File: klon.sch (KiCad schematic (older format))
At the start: 71 parts, among them SW1 SW_DPDT_x2, U1 TL072, U2 LTC1044, U3 TL072

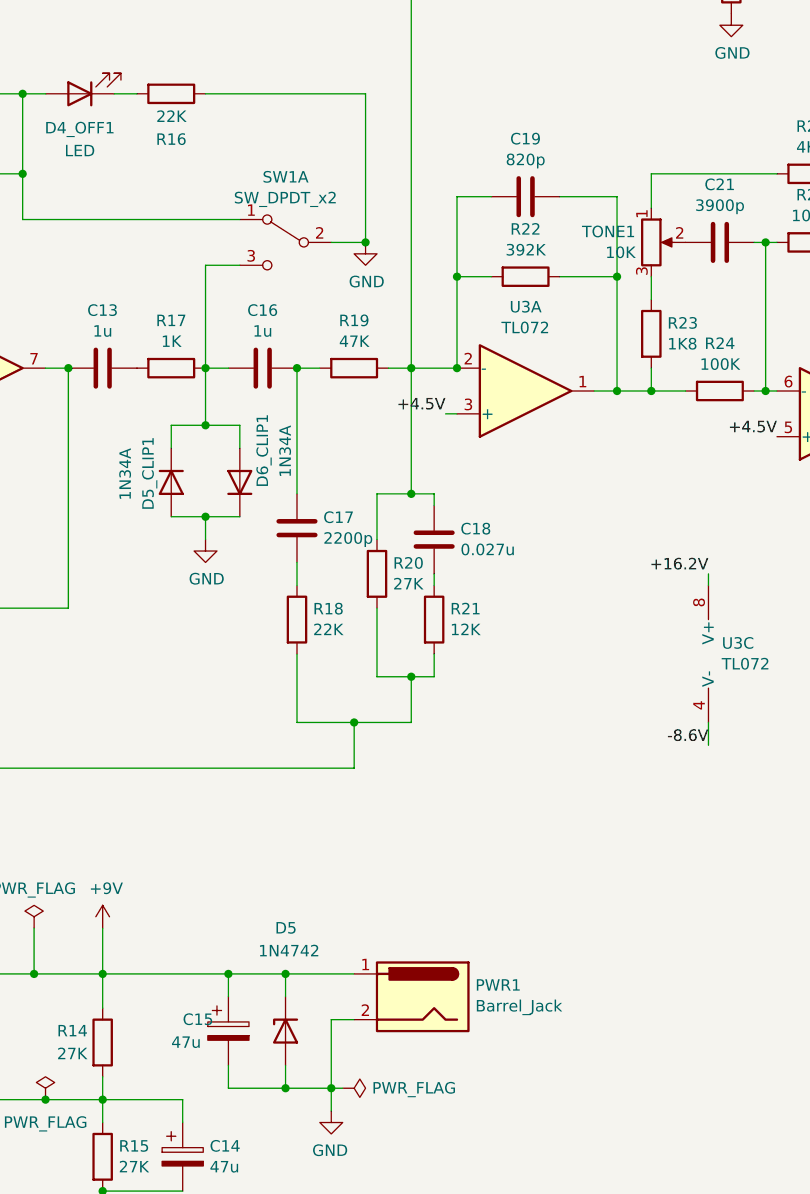
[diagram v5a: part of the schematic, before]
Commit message: fix power polarity, new PCB layout
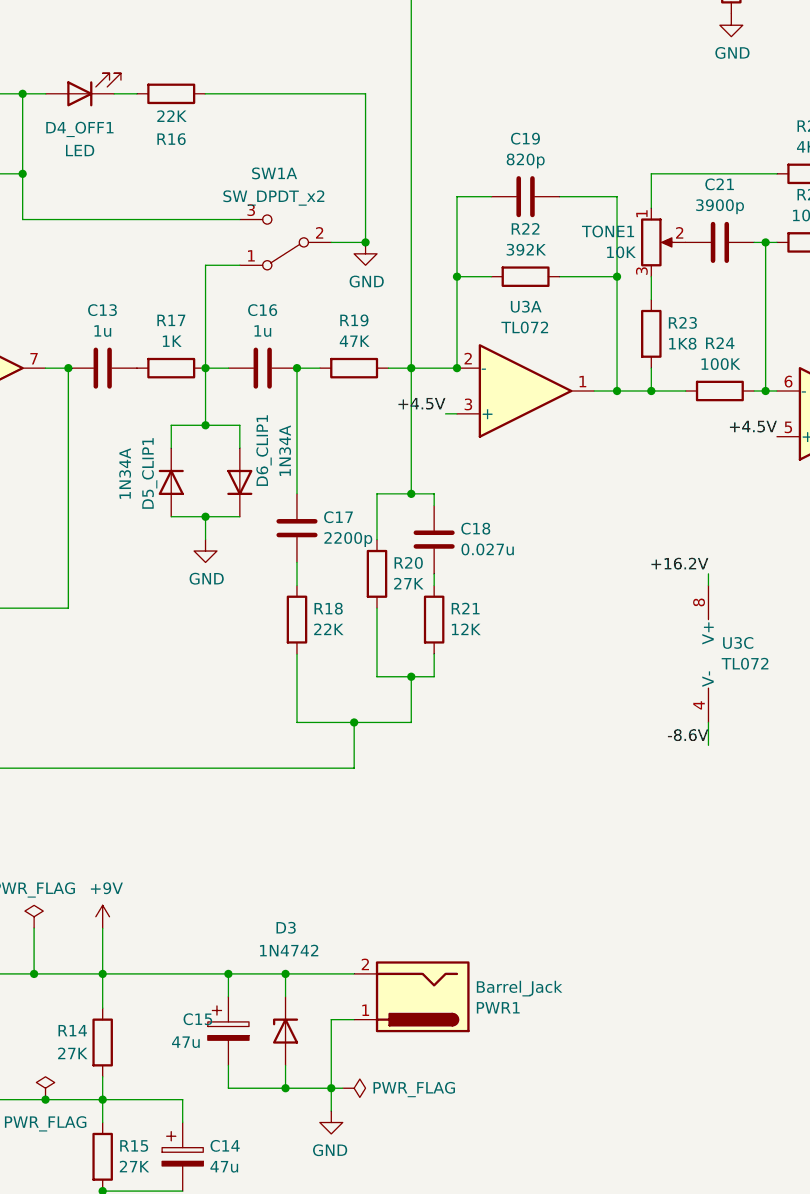
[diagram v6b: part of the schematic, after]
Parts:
- C8: footprint Capacitor_THT:C_Rect_L7.0mm_W3.5mm_P5.00mm -> Capacitor_THT:C_Rect_L7.0mm_W2.0mm_P5.00mm
- D3: renamed from D5; footprint Diode_THT:D_DO-34_SOD68_P7.62mm_Horizontal -> Diode_THT:D_DO-34_SOD68_P10.16mm_Horizontal
- GAIN_1: footprint Potentiometer_THT:Potentiometer_Alpha_RD902F-40-00D_Dual_Vertical_CircularHoles -> Connector_PinHeader_2.54mm:PinHeader_2x03_P2.54mm_Vertical
- SW1: footprint Connector_PinHeader_1.27mm:PinHeader_2x03_P1.27mm_Vertical -> Connector_PinHeader_2.54mm:PinHeader_2x03_P2.54mm_Vertical
- TONE1, VOL1: footprint Potentiometer_THT:Potentiometer_Alpha_RD901F-40-00D_Single_Vertical_CircularHoles -> Connector_PinHeader_2.54mm:PinHeader_1x03_P2.54mm_Vertical
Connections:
- net +9V: now also PWR1.2; no longer PWR1.1
- net GND: now also PWR1.1; no longer PWR1.2
- net at C16.2, D5_CLIP1.1 (K), D6_CLIP1.2 (A)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: now also SW1.1 (A); no longer SW1.3 (C)
- net at D4_OFF1.2 (A), R12.2, R13.1: now also SW1.3 (C); no longer SW1.1 (A)
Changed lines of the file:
@@
 F 0 "C8" V 2898 2950 50  0000 C CNN
 F 1 "0.068u" V 2989 2950 50  0000 C CNN
-F 2 "Capacitor_THT:C_Rect_L7.0mm_W3.5mm_P5.00mm" H 3188 2800 50  0001 C CNN
+F 2 "Capacitor_THT:C_Rect_L7.0mm_W2.0mm_P5.00mm" H 3188 2800 50  0001 C CNN
 F 3 "~" H 3150 2950 50  0001 C CNN
 	1    3150 2950
@@
 F 0 "GAIN_1" H 3281 4846 50  0000 R CNN
 F 1 "100K" H 3281 4755 50  0000 R CNN
-F 2 "Potentiometer_THT:Potentiometer_Alpha_RD902F-40-00D_Dual_Vertical_CircularHoles" H 3350 4800 50  0001 C CNN
+F 2 "Connector_PinHeader_2.54mm:PinHeader_2x03_P2.54mm_Vertical" H 3350 4800 50  0001 C CNN
 F 3 "~" H 3350 4800 50  0001 C CNN
 	1    3350 4800
@@
 $EndComp
 $Comp
-L power:GND #PWR07
+L power:GND #PWR06
 U 1 1 60CF8CE7
 P 3250 1750
-F 0 "#PWR07" H 3250 1500 50  0001 C CNN
+F 0 "#PWR06" H 3250 1500 50  0001 C CNN
 F 1 "GND" H 3255 1577 50  0000 C CNN
 F 2 "" H 3250 1750 50  0001 C CNN
@@
 F 0 "TONE1" H 7631 2546 50  0000 R CNN
 F 1 "10K" H 7631 2455 50  0000 R CNN
-F 2 "Potentiometer_THT:Potentiometer_Alpha_RD901F-40-00D_Single_Vertical_CircularHoles" H 7700 2500 50  0001 C CNN
+F 2 "Connector_PinHeader_2.54mm:PinHeader_1x03_P2.54mm_Vertical" H 7700 2500 50  0001 C CNN
 F 3 "~" H 7700 2500 50  0001 C CNN
 	1    7700 2500
@@
 F 0 "VOL1" H 9431 3546 50  0000 R CNN
 F 1 "10K" H 9431 3455 50  0000 R CNN
-F 2 "Potentiometer_THT:Potentiometer_Alpha_RD901F-40-00D_Single_Vertical_CircularHoles" H 9500 3500 50  0001 C CNN
+F 2 "Connector_PinHeader_2.54mm:PinHeader_1x03_P2.54mm_Vertical" H 9500 3500 50  0001 C CNN
 F 3 "~" H 9500 3500 50  0001 C CNN
 	1    9500 3500
@@
 $EndComp
 $Comp
-L power:GND #PWR016
+L power:GND #PWR015
 U 1 1 60DC01EF
 P 9500 3750
-F 0 "#PWR016" H 9500 3500 50  0001 C CNN
+F 0 "#PWR015" H 9500 3500 50  0001 C CNN
 F 1 "GND" H 9505 3577 50  0000 C CNN
 F 2 "" H 9500 3750 50  0001 C CNN
@@
 Connection ~ 8050 1100
 $Comp
-L power:GND #PWR015
+L power:GND #PWR014
 U 1 1 60E2597F
 P 8050 1500
-F 0 "#PWR015" H 8050 1250 50  0001 C CNN
+F 0 "#PWR014" H 8050 1250 50  0001 C CNN
 F 1 "GND" H 8055 1327 50  0000 C CNN
 F 2 "" H 8050 1500 50  0001 C CNN
@@
 $EndComp
 $Comp
-L power:GND #PWR017
+L power:GND #PWR016
 U 1 1 60E40ABE
 P 10500 4000
-F 0 "#PWR017" H 10500 3750 50  0001 C CNN
+F 0 "#PWR016" H 10500 3750 50  0001 C CNN
 F 1 "GND" H 10505 3827 50  0000 C CNN
 F 2 "" H 10500 4000 50  0001 C CNN
@@
 	5600 3700 5750 3700
 $Comp
-L power:GND #PWR012
+L power:GND #PWR011
 U 1 1 60CDC483
 P 5750 3800
-F 0 "#PWR012" H 5750 3550 50  0001 C CNN
+F 0 "#PWR011" H 5750 3550 50  0001 C CNN
 F 1 "GND" H 5755 3627 50  0000 C CNN
 F 2 "" H 5750 3800 50  0001 C CNN
@@
 	10300 3400 10500 3400
 $Comp
-L power:GND #PWR013
+L power:GND #PWR012
 U 1 1 6116E861
 P 6300 6300
-F 0 "#PWR013" H 6300 6050 50  0001 C CNN
+F 0 "#PWR012" H 6300 6050 50  0001 C CNN
 F 1 "GND" H 6305 6127 50  0000 C CNN
 F 2 "" H 6300 6300 50  0001 C CNN
@@
 $EndComp
 $Comp
-L Device:D_Zener D5
+L Device:D_Zener D3
 U 1 1 6117C2F3
 P 6100 5950
-F 0 "D5" V 5650 5900 50  0000 L CNN
+F 0 "D3" V 5650 5900 50  0000 L CNN
 F 1 "1N4742" V 5750 5800 50  0000 L CNN
-F 2 "Diode_THT:D_DO-34_SOD68_P7.62mm_Horizontal" H 6100 5950 50  0001 C CNN
+F 2 "Diode_THT:D_DO-34_SOD68_P10.16mm_Horizontal" H 6100 5950 50  0001 C CNN
 F 3 "~" H 6100 5950 50  0001 C CNN
 	1    6100 5950
@@
 $EndComp
 $Comp
-L power:GND #PWR05
+L power:GND #PWR04
 U 1 1 612C633A
 P 1850 7050
-F 0 "#PWR05" H 1850 6800 50  0001 C CNN
+F 0 "#PWR04" H 1850 6800 50  0001 C CNN
 F 1 "GND" H 1855 6877 50  0000 C CNN
 F 2 "" H 1850 7050 50  0001 C CNN
@@
 	4450 6750 3150 6750
 $Comp
-L power:GND #PWR06
+L power:GND #PWR05
 U 1 1 6132C604
 P 2200 6100
-F 0 "#PWR06" H 2200 5850 50  0001 C CNN
+F 0 "#PWR05" H 2200 5850 50  0001 C CNN
 F 1 "GND" H 2205 5927 50  0000 C CNN
 F 2 "" H 2200 6100 50  0001 C CNN
@@
 $EndComp
 $Comp
-L power:GND #PWR011
+L power:GND #PWR010
 U 1 1 6139B14F
 P 5300 6750
-F 0 "#PWR011" H 5300 6500 50  0001 C CNN
+F 0 "#PWR010" H 5300 6500 50  0001 C CNN
 F 1 "GND" H 5305 6577 50  0000 C CNN
 F 2 "" H 5300 6750 50  0001 C CNN
@@
 +4.5V
 $Comp
-L power:+9V #PWR010
+L power:+9V #PWR09
 U 1 1 614332A8
 P 5300 5500
-F 0 "#PWR010" H 5300 5350 50  0001 C CNN
+F 0 "#PWR09" H 5300 5350 50  0001 C CNN
 F 1 "+9V" H 5315 5673 50  0000 C CNN
 F 2 "" H 5300 5500 50  0001 C CNN
@@
 	4450 5700 4450 6750
 $Comp
-L power:GND #PWR08
+L power:GND #PWR07
 U 1 1 6154C007
 P 3850 6400
-F 0 "#PWR08" H 3850 6150 50  0001 C CNN
+F 0 "#PWR07" H 3850 6150 50  0001 C CNN
 F 1 "GND" H 3855 6227 50  0000 C CNN
 F 2 "" H 3850 6400 50  0001 C CNN
@@
 F 0 "SW1" H 10000 3075 50  0000 C CNN
 F 1 "SW_DPDT_x2" H 10000 3166 50  0000 C CNN
-F 2 "Connector_PinHeader_1.27mm:PinHeader_2x03_P1.27mm_Vertical" H 10000 3400 50  0001 C CNN
+F 2 "Connector_PinHeader_2.54mm:PinHeader_2x03_P2.54mm_Vertical" H 10000 3400 50  0001 C CNN
 F 3 "~" H 10000 3400 50  0001 C CNN
 	2    10000 3400
@@
 U 1 1 6160C4D4
 P 6100 2500
-F 0 "SW1" H 6100 2785 50  0000 C CNN
-F 1 "SW_DPDT_x2" H 6100 2694 50  0000 C CNN
-F 2 "Connector_PinHeader_1.27mm:PinHeader_2x03_P1.27mm_Vertical" H 6100 2500 50  0001 C CNN
+F 0 "SW1" H 6150 2200 50  0000 C CNN
+F 1 "SW_DPDT_x2" H 6150 2300 50  0000 C CNN
+F 2 "Connector_PinHeader_2.54mm:PinHeader_2x03_P2.54mm_Vertical" H 6100 2500 50  0001 C CNN
 F 3 "~" H 6100 2500 50  0001 C CNN
 	1    6100 2500
-	-1   0    0    -1
-$EndComp
-$Comp
-L power:GND #PWR014
+	-1   0    0    1
+$EndComp
+$Comp
+L power:GND #PWR013
 U 1 1 61610015
 P 6450 2500
-F 0 "#PWR014" H 6450 2250 50  0001 C CNN
+F 0 "#PWR013" H 6450 2250 50  0001 C CNN
 F 1 "GND" H 6455 2327 50  0000 C CNN
 F 2 "" H 6450 2500 50  0001 C CNN
@@
 	6450 2500 6300 2500
 $Comp
-L power:+9V #PWR09
+L power:+9V #PWR08
 U 1 1 6161D720
 P 4000 1850
-F 0 "#PWR09" H 4000 1700 50  0001 C CNN
+F 0 "#PWR08" H 4000 1700 50  0001 C CNN
 F 1 "+9V" V 4015 1978 50  0000 L CNN
 F 2 "" H 4000 1850 50  0001 C CNN
@@
 F 0 "GAIN_1" H 3480 3554 50  0000 R CNN
 F 1 "100K" H 3480 3645 50  0000 R CNN
-F 2 "Potentiometer_THT:Potentiometer_Alpha_RD902F-40-00D_Dual_Vertical_CircularHoles" H 3550 3600 50  0001 C CNN
+F 2 "Connector_PinHeader_2.54mm:PinHeader_2x03_P2.54mm_Vertical" H 3550 3600 50  0001 C CNN
 F 3 "~" H 3550 3600 50  0001 C CNN
 	2    3550 3600
@@
 F 3 "~" H 6750 5760 50  0001 C CNN
 	1    6700 5800
-	-1   0    0    -1
-$EndComp
-Wire Wire Line
+	-1   0    0    1
+$EndComp
+Wire Wire Line

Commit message: update pcb layout
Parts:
- renumbered D3_ON1 to D3_ON, D4_OFF1 to D4_OFF, GAIN_1 to GAIN, SW1 to SW, TONE1 to TONE, VOL1 to VOL
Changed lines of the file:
@@
 	3400 2950 3300 2950
 $Comp
-L klon-rescue:R_POT_Dual_Separate-Device GAIN_1
+L klon-rescue:R_POT_Dual_Separate-Device GAIN
 U 1 1 60CBA9B6
 P 3350 4800
-F 0 "GAIN_1" H 3281 4846 50  0000 R CNN
+F 0 "GAIN" H 3281 4846 50  0000 R CNN
 F 1 "100K" H 3281 4755 50  0000 R CNN
 F 2 "Connector_PinHeader_2.54mm:PinHeader_2x03_P2.54mm_Vertical" H 3350 4800 50  0001 C CNN
@@
 Connection ~ 7550 2650
 $Comp
-L klon-rescue:R_POT-Device TONE1
+L klon-rescue:R_POT-Device TONE
 U 1 1 60D788AD
 P 7700 2500
-F 0 "TONE1" H 7631 2546 50  0000 R CNN
+F 0 "TONE" H 7631 2546 50  0000 R CNN
 F 1 "10K" H 7631 2455 50  0000 R CNN
 F 2 "Connector_PinHeader_2.54mm:PinHeader_1x03_P2.54mm_Vertical" H 7700 2500 50  0001 C CNN
@@
 $EndComp
 $Comp
-L klon-rescue:R_POT-Device VOL1
+L klon-rescue:R_POT-Device VOL
 U 1 1 60DBED2B
 P 9500 3500
-F 0 "VOL1" H 9431 3546 50  0000 R CNN
+F 0 "VOL" H 9431 3546 50  0000 R CNN
 F 1 "10K" H 9431 3455 50  0000 R CNN
 F 2 "Connector_PinHeader_2.54mm:PinHeader_1x03_P2.54mm_Vertical" H 9500 3500 50  0001 C CNN
@@
 	4250 5700 4450 5700
 $Comp
-L Switch:SW_DPDT_x2 SW1
+L Switch:SW_DPDT_x2 SW
 U 2 1 6160A4D6
 P 10000 3400
-F 0 "SW1" H 10000 3075 50  0000 C CNN
+F 0 "SW" H 10000 3075 50  0000 C CNN
 F 1 "SW_DPDT_x2" H 10000 3166 50  0000 C CNN
 F 2 "Connector_PinHeader_2.54mm:PinHeader_2x03_P2.54mm_Vertical" H 10000 3400 50  0001 C CNN
@@
 $EndComp
 $Comp
-L Switch:SW_DPDT_x2 SW1
+L Switch:SW_DPDT_x2 SW
 U 1 1 6160C4D4
 P 6100 2500
-F 0 "SW1" H 6150 2200 50  0000 C CNN
+F 0 "SW" H 6150 2200 50  0000 C CNN
 F 1 "SW_DPDT_x2" H 6150 2300 50  0000 C CNN
 F 2 "Connector_PinHeader_2.54mm:PinHeader_2x03_P2.54mm_Vertical" H 6100 2500 50  0001 C CNN
@@
 	6650 1400 6650 3050
 $Comp
-L Device:LED D3_ON1
+L Device:LED D3_ON
 U 1 1 6161B08C
 P 4250 1850
-F 0 "D3_ON1" H 4243 2067 50  0000 C CNN
+F 0 "D3_ON" H 4243 2067 50  0000 C CNN
 F 1 "LED" H 4243 1976 50  0000 C CNN
 F 2 "LED_THT:LED_D3.0mm_Clear" H 4250 1850 50  0001 C CNN
@@
 Connection ~ 4950 2200
 $Comp
-L klon-rescue:R_POT_Dual_Separate-Device GAIN_1
+L klon-rescue:R_POT_Dual_Separate-Device GAIN
 U 2 1 60CB9AA2
 P 3550 3600
-F 0 "GAIN_1" H 3480 3554 50  0000 R CNN
+F 0 "GAIN" H 3480 3554 50  0000 R CNN
 F 1 "100K" H 3480 3645 50  0000 R CNN
 F 2 "Connector_PinHeader_2.54mm:PinHeader_2x03_P2.54mm_Vertical" H 3550 3600 50  0001 C CNN
@@
 	6150 4000 6150 3900
 $Comp
-L Device:LED D4_OFF1
+L Device:LED D4_OFF
 U 1 1 61235DB3
 P 5200 1850
-F 0 "D4_OFF1" H 5200 2000 50  0000 C CNN
+F 0 "D4_OFF" H 5200 2000 50  0000 C CNN
 F 1 "LED" H 5200 2100 50  0000 C CNN
 F 2 "LED_THT:LED_D3.0mm_Clear" H 5200 1850 50  0001 C CNN
